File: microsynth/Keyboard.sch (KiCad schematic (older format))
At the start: 54 parts, among them J5 Conn_01x02_Male, Q1 BC182, Q2 BC182L, SW1-DRIFT1 DRIFT, SW9 TRIGGER, U1 RC4136, U2 TL072, U3 4011, U4 4016, U5 LF347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

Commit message: Change switch footprints
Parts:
- SW9: footprint Buttons_Switches_ThroughHole:DP3T_Toggle -> Buttons_Switches_ThroughHole:L203011MS02Q
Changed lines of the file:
@@
 F 0 "SW9" H 2750 3850 50  0000 L CNN
 F 1 "TRIGGER" H 2750 3750 50  0000 L CNN
-F 2 "Buttons_Switches_ThroughHole:DP3T_Toggle" H 2550 3700 50  0001 C CNN
+F 2 "Buttons_Switches_ThroughHole:L203011MS02Q" H 2550 3700 50  0001 C CNN
 F 3 "" H 2550 3700 50  0001 C CNN
 	2    2550 3700

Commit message: Layout...-3
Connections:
- net +VSW: now also SW9.2; no longer SW9.6
- net TO_S9A_KEYBOARD_CONTROLLER: now also SW9.4; no longer SW9.8
- new net: SW9.1, SW9.3, U3.2
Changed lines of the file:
@@
 $EndComp
 $Comp
-L power:GND #PWR0200
+L power:GND #PWR?
 U 1 1 5E8D13DA
 P 5600 2850
-F 0 "#PWR0200" H 5600 2600 50  0001 C CNN
+F 0 "#PWR?" H 5600 2600 50  0001 C CNN
 F 1 "GND" H 5605 2677 50  0000 C CNN
 F 2 "" H 5600 2850 50  0001 C CNN
@@
 	1850 3350 1850 3200
 $Comp
-L power:+VSW #PWR0201
+L power:+VSW #PWR?
 U 1 1 5E8EF5B5
 P 1850 3200
-F 0 "#PWR0201" H 1850 3050 50  0001 C CNN
+F 0 "#PWR?" H 1850 3050 50  0001 C CNN
 F 1 "+VSW" H 1865 3373 50  0000 C CNN
 F 2 "" H 1850 3200 50  0001 C CNN
@@
 	1200 2250 1300 2250
 $Comp
-L power:GND #PWR0202
+L power:GND #PWR?
 U 1 1 5E8F614B
 P 850 2350
-F 0 "#PWR0202" H 850 2100 50  0001 C CNN
+F 0 "#PWR?" H 850 2100 50  0001 C CNN
 F 1 "GND" H 855 2177 50  0000 C CNN
 F 2 "" H 850 2350 50  0001 C CNN
@@
 Connection ~ 850  2250
 $Comp
-L power:+VSW #PWR0203
+L power:+VSW #PWR?
 U 1 1 5E8F7B80
 P 850 2750
-F 0 "#PWR0203" H 850 2600 50  0001 C CNN
+F 0 "#PWR?" H 850 2600 50  0001 C CNN
 F 1 "+VSW" H 865 2923 50  0000 C CNN
 F 2 "" H 850 2750 50  0001 C CNN
@@
 $EndComp
 $Comp
-L power:GND #PWR0204
+L power:GND #PWR?
 U 1 1 5E8F97A9
 P 850 3500
-F 0 "#PWR0204" H 850 3250 50  0001 C CNN
+F 0 "#PWR?" H 850 3250 50  0001 C CNN
 F 1 "GND" H 855 3327 50  0000 C CNN
 F 2 "" H 850 3500 50  0001 C CNN
@@
 Connection ~ 5600 2150
 $Comp
-L power:GND #PWR0205
+L power:GND #PWR?
 U 1 1 5E9133C8
 P 900 850
-F 0 "#PWR0205" H 900 600 50  0001 C CNN
+F 0 "#PWR?" H 900 600 50  0001 C CNN
 F 1 "GND" H 905 677 50  0000 C CNN
 F 2 "" H 900 850 50  0001 C CNN
@@
 	900  850  1300 850
 $Comp
-L power:-VSW #PWR0206
+L power:-VSW #PWR?
 U 1 1 5E914B3C
 P 800 1250
-F 0 "#PWR0206" H 800 1350 50  0001 C CNN
+F 0 "#PWR?" H 800 1350 50  0001 C CNN
 F 1 "-VSW" H 815 1423 50  0000 C CNN
 F 2 "" H 800 1250 50  0001 C CNN
@@
 $EndComp
 $Comp
-L power:+VSW #PWR0207
+L power:+VSW #PWR?
 U 1 1 5E91C344
 P 4850 850
-F 0 "#PWR0207" H 4850 700 50  0001 C CNN
+F 0 "#PWR?" H 4850 700 50  0001 C CNN
 F 1 "+VSW" H 4865 1023 50  0000 C CNN
 F 2 "" H 4850 850 50  0001 C CNN
@@
 	6000 1250 5800 1250
 $Comp
-L power:-VSW #PWR0208
+L power:-VSW #PWR?
 U 1 1 5E92F178
 P 6750 1000
-F 0 "#PWR0208" H 6750 1100 50  0001 C CNN
+F 0 "#PWR?" H 6750 1100 50  0001 C CNN
 F 1 "-VSW" H 6765 1173 50  0000 C CNN
 F 2 "" H 6750 1000 50  0001 C CNN
@@
 	7000 1300 7000 1350
 $Comp
-L power:+VSW #PWR0209
+L power:+VSW #PWR?
 U 1 1 5E93EA0A
 P 7450 1000
-F 0 "#PWR0209" H 7450 850 50  0001 C CNN
+F 0 "#PWR?" H 7450 850 50  0001 C CNN
 F 1 "+VSW" H 7465 1173 50  0000 C CNN
 F 2 "" H 7450 1000 50  0001 C CNN
@@
 	7000 2000 7000 1800
 $Comp
-L power:GND #PWR0210
+L power:GND #PWR?
 U 1 1 5E94D6E3
 P 9000 1950
-F 0 "#PWR0210" H 9000 1700 50  0001 C CNN
+F 0 "#PWR?" H 9000 1700 50  0001 C CNN
 F 1 "GND" H 9005 1777 50  0000 C CNN
 F 2 "" H 9000 1950 50  0001 C CNN
@@
 Connection ~ 9400 1900
 $Comp
-L power:-VSW #PWR0211
+L power:-VSW #PWR?
 U 1 1 5E956780
 P 9400 850
-F 0 "#PWR0211" H 9400 950 50  0001 C CNN
+F 0 "#PWR?" H 9400 950 50  0001 C CNN
 F 1 "-VSW" H 9415 1023 50  0000 C CNN
 F 2 "" H 9400 850 50  0001 C CNN
@@
 	10250 2500 10400 2500
 $Comp
-L power:GND #PWR0212
+L power:GND #PWR?
 U 1 1 5E9679B4
 P 9950 3350
-F 0 "#PWR0212" H 9950 3100 50  0001 C CNN
+F 0 "#PWR?" H 9950 3100 50  0001 C CNN
 F 1 "GND" H 9955 3177 50  0000 C CNN
 F 2 "" H 9950 3350 50  0001 C CNN
@@
 	6850 3550 6850 3650
 $Comp
-L power:GND #PWR0213
+L power:GND #PWR?
 U 1 1 5E9F4545
 P 7250 3700
-F 0 "#PWR0213" H 7250 3450 50  0001 C CNN
+F 0 "#PWR?" H 7250 3450 50  0001 C CNN
 F 1 "GND" H 7255 3527 50  0000 C CNN
 F 2 "" H 7250 3700 50  0001 C CNN
@@
 Connection ~ 6400 3550
 $Comp
-L power:-VSW #PWR0214
+L power:-VSW #PWR?
 U 1 1 5EA12F1F
 P 6850 4500
-F 0 "#PWR0214" H 6850 4600 50  0001 C CNN
+F 0 "#PWR?" H 6850 4600 50  0001 C CNN
 F 1 "-VSW" H 6865 4673 50  0000 C CNN
 F 2 "" H 6850 4500 50  0001 C CNN
@@
 	6850 4500 6850 4450
 $Comp
-L power:+VSW #PWR0215
+L power:+VSW #PWR?
 U 1 1 5EA199A7
 P 6850 2700
-F 0 "#PWR0215" H 6850 2550 50  0001 C CNN
+F 0 "#PWR?" H 6850 2550 50  0001 C CNN
 F 1 "+VSW" H 6865 2873 50  0000 C CNN
 F 2 "" H 6850 2700 50  0001 C CNN
@@
 	6850 2700 6850 2800
 $Comp
-L power:GND #PWR0216
+L power:GND #PWR?
 U 1 1 5EA216DE
 P 7400 2700
-F 0 "#PWR0216" H 7400 2450 50  0001 C CNN
+F 0 "#PWR?" H 7400 2450 50  0001 C CNN
 F 1 "GND" H 7405 2527 50  0000 C CNN
 F 2 "" H 7400 2700 50  0001 C CNN
@@
 Connection ~ 8150 2350
 $Comp
-L power:+VSW #PWR0217
+L power:+VSW #PWR?
 U 1 1 5EA466FB
 P 4750 2500
-F 0 "#PWR0217" H 4750 2350 50  0001 C CNN
+F 0 "#PWR?" H 4750 2350 50  0001 C CNN
 F 1 "+VSW" H 4765 2673 50  0000 C CNN
 F 2 "" H 4750 2500 50  0001 C CNN
@@
 $EndComp
 $Comp
-L power:-VSW #PWR0218
+L power:-VSW #PWR?
 U 1 1 5EA46F8D
 P 4750 2800
-F 0 "#PWR0218" H 4750 2900 50  0001 C CNN
+F 0 "#PWR?" H 4750 2900 50  0001 C CNN
 F 1 "-VSW" H 4765 2973 50  0000 C CNN
 F 2 "" H 4750 2800 50  0001 C CNN
@@
 NoConn ~ 8750 2800
 $Comp
-L power:-VSW #PWR0219
+L power:-VSW #PWR?
 U 1 1 5EA96E7C
 P 8550 2800
-F 0 "#PWR0219" H 8550 2900 50  0001 C CNN
+F 0 "#PWR?" H 8550 2900 50  0001 C CNN
 F 1 "-VSW" H 8565 2973 50  0000 C CNN
 F 2 "" H 8550 2800 50  0001 C CNN
@@
 $EndComp
 $Comp
-L power:+VSW #PWR0220
+L power:+VSW #PWR?
 U 1 1 5EA97787
 P 8550 2200
-F 0 "#PWR0220" H 8550 2050 50  0001 C CNN
+F 0 "#PWR?" H 8550 2050 50  0001 C CNN
 F 1 "+VSW" H 8565 2373 50  0000 C CNN
 F 2 "" H 8550 2200 50  0001 C CNN
@@
 $Comp
 L microsynth-rescue:SW_DPTT_SELECTOR-Switch SW9
-U 2 1 5E96003B
+U 1 1 5E96003B
 P 2550 3700
 F 0 "SW9" H 2750 3850 50  0000 L CNN
@@
 F 2 "Buttons_Switches_ThroughHole:L203011MS02Q" H 2550 3700 50  0001 C CNN
 F 3 "" H 2550 3700 50  0001 C CNN
-	2    2550 3700
-	1    0    0    -1
+	1    2550 3700
+	1    0    0    1
 $EndComp
 $Comp
@@
 $EndComp
 $Comp
-L power:+VSW #PWR0232
+L power:+VSW #PWR?
 U 1 1 5E896D52
 P 9200 4350
-F 0 "#PWR0232" H 9200 4200 50  0001 C CNN
+F 0 "#PWR?" H 9200 4200 50  0001 C CNN
 F 1 "+VSW" H 9200 4450 50  0000 C CNN
 F 2 "" H 9200 4350 50  0001 C CNN
@@
 $EndComp
 $Comp
-L power:-VSW #PWR0233
+L power:-VSW #PWR?
 U 1 1 5E8967F9
 P 9200 5050
-F 0 "#PWR0233" H 9200 5150 50  0001 C CNN
+F 0 "#PWR?" H 9200 5150 50  0001 C CNN
 F 1 "-VSW" H 9215 5223 50  0000 C CNN
 F 2 "" H 9200 5050 50  0001 C CNN
@@
 Connection ~ 6400 2250
 $Comp
-L power:+VSW #PWR0234
+L power:+VSW #PWR?
 U 1 1 5E8EBE3F
 P 9650 4400
-F 0 "#PWR0234" H 9650 4250 50  0001 C CNN
+F 0 "#PWR?" H 9650 4250 50  0001 C CNN
 F 1 "+VSW" H 9650 4500 50  0000 C CNN
 F 2 "" H 9650 4400 50  0001 C CNN
@@
 $EndComp
 $Comp
-L power:-VSW #PWR0235
+L power:-VSW #PWR?
 U 1 1 5E8EC49A
 P 9650 5000
-F 0 "#PWR0235" H 9650 5100 50  0001 C CNN
+F 0 "#PWR?" H 9650 5100 50  0001 C CNN
 F 1 "-VSW" H 9665 5173 50  0000 C CNN
 F 2 "" H 9650 5000 50  0001 C CNN
@@
 $EndComp
 $Comp
-L power:+VSW #PWR0236
+L power:+VSW #PWR?
 U 1 1 5EC4CC4F
 P 10050 4400
-F 0 "#PWR0236" H 10050 4250 50  0001 C CNN
+F 0 "#PWR?" H 10050 4250 50  0001 C CNN
 F 1 "+VSW" H 10050 4500 50  0000 C CNN
 F 2 "" H 10050 4400 50  0001 C CNN
@@
 $EndComp
 $Comp
-L power:-VSW #PWR0237
+L power:-VSW #PWR?
 U 1 1 5EC4D1BE
 P 10050 5000
-F 0 "#PWR0237" H 10050 5100 50  0001 C CNN
+F 0 "#PWR?" H 10050 5100 50  0001 C CNN
 F 1 "-VSW" H 10065 5173 50  0000 C CNN
 F 2 "" H 10050 5000 50  0001 C CNN
@@
 	8150 2150 8150 2350
 $Comp
-L power:-VSW #PWR0228
+L power:-VSW #PWR?
 U 1 1 5E98AA20
 P 6350 1000
-F 0 "#PWR0228" H 6350 1100 50  0001 C CNN
+F 0 "#PWR?" H 6350 1100 50  0001 C CNN
 F 1 "-VSW" H 6365 1173 50  0000 C CNN
 F 2 "" H 6350 1000 50  0001 C CNN
@@
 $EndComp
 $Comp
-L power:-VSW #PWR0229
+L power:-VSW #PWR?
 U 1 1 5E98AE00
 P 6550 1000
-F 0 "#PWR0229" H 6550 1100 50  0001 C CNN
+F 0 "#PWR?" H 6550 1100 50  0001 C CNN
 F 1 "-VSW" H 6565 1173 50  0000 C CNN
 F 2 "" H 6550 1000 50  0001 C CNN

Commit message: Tidy up, name switches, proper footprints for all trimmers
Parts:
- SW1-DRIFT1, SW9: footprint Buttons_Switches_ThroughHole:L203011MS02Q -> Buttons_Switches_ThroughHole:G-1128S-1110
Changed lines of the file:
@@
 F 0 "SW1" H 5844 1083 50  0000 L CNN
 F 1 "DRIFT" H 5844 992 50  0000 L CNN
-F 2 "Buttons_Switches_ThroughHole:L203011MS02Q" H 5650 1050 50  0001 C CNN
+F 2 "Buttons_Switches_ThroughHole:G-1128S-1110" H 5650 1050 50  0001 C CNN
 F 3 "https://www.tme.eu/Document/aa2d40399ed88e2cc02320a01dfb97ce/OSseries.pdf" H 5650 1050 50  0001 C CNN
 F 4 "DRIFT" H 5844 901 50  0000 L CNN "Label"
@@
 F 0 "SW9" H 2750 3850 50  0000 L CNN
 F 1 "TRIGGER" H 2750 3750 50  0000 L CNN
-F 2 "Buttons_Switches_ThroughHole:L203011MS02Q" H 2550 3700 50  0001 C CNN
+F 2 "Buttons_Switches_ThroughHole:G-1128S-1110" H 2550 3700 50  0001 C CNN
 F 3 "" H 2550 3700 50  0001 C CNN
 	1    2550 3700

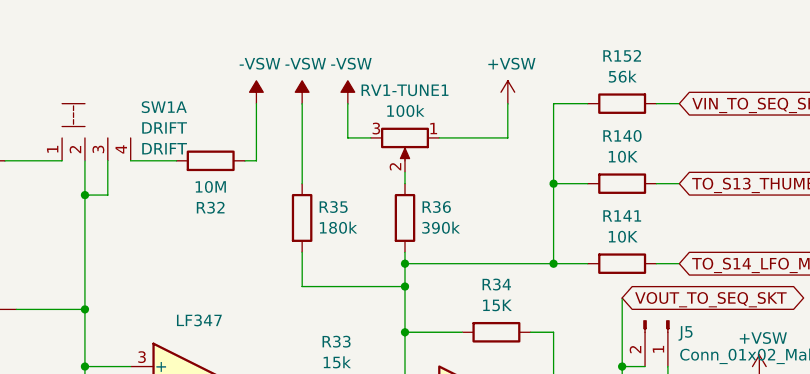
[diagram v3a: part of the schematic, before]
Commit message: Replace switches in schematic, add extra octave to VCO
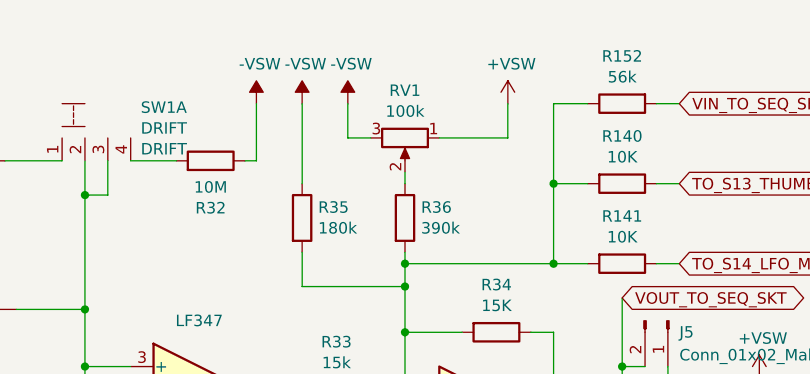
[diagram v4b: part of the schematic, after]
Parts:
- renumbered RV1-TUNE1 to RV1
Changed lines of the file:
@@
 	7000 1800 7000 1700
 $Comp
-L Device:R_POT RV1-TUNE1
+L Device:R_POT RV1
 U 1 1 5E936F79
 P 7000 1150
-F 0 "RV1-TUNE1" V 6793 1150 50  0000 C CNN
+F 0 "RV1" V 6793 1150 50  0000 C CNN
 F 1 "100k" V 6884 1150 50  0000 C CNN
 F 2 "Potentiometers:Potentiometer_Trimmer_Bourns_PV36W" H 7000 1150 50  0001 C CNN

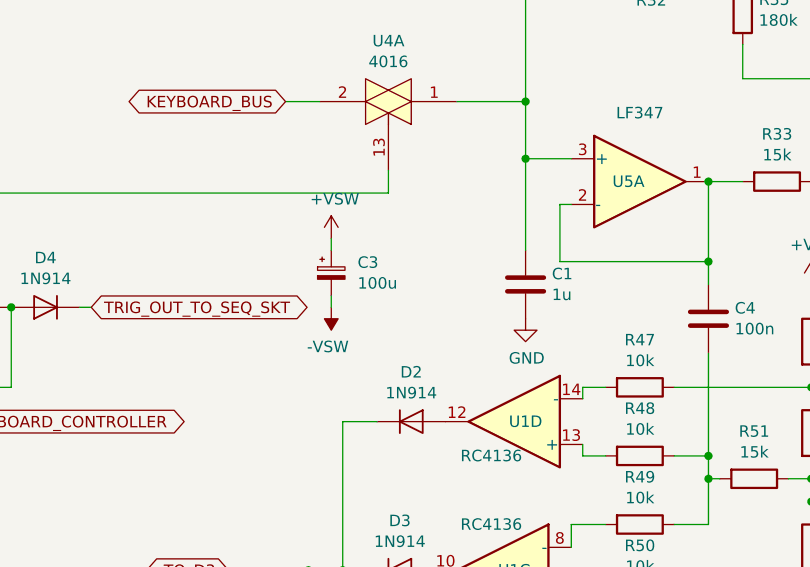
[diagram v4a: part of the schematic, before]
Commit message: Proper capacitor footprints
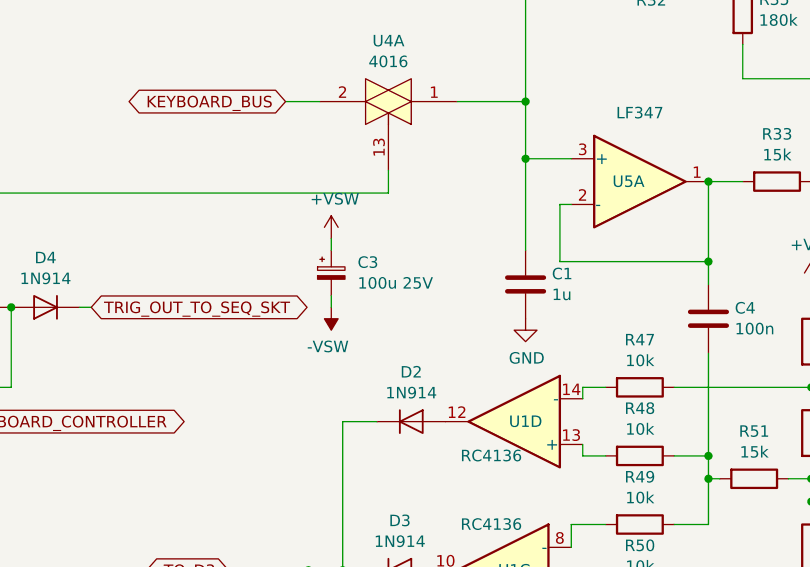
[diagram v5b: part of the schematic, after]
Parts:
- C1: footprint Capacitor_THT:C_Disc_D5.0mm_W2.5mm_P5.00mm -> Capacitor_THT:C_Rect_L7.2mm_W7.2mm_P5.00mm_FKS2_FKP2_MKS2_MKP2
- C2, C4, C6, C7: footprint Capacitor_THT:C_Disc_D5.0mm_W2.5mm_P5.00mm -> Capacitor_THT:C_Rect_L7.2mm_W2.5mm_P5.00mm_FKS2_FKP2_MKS2_MKP2
- C3: value 100u -> 100u 25V
- C5: footprint Capacitor_THT:C_Disc_D5.0mm_W2.5mm_P5.00mm -> Capacitor_THT:C_Rect_L7.2mm_W4.5mm_P5.00mm_FKS2_FKP2_MKS2_MKP2
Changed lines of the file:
@@
 F 0 "C6" H 9815 1696 50  0000 L CNN
 F 1 "10n" H 9815 1605 50  0000 L CNN
-F 2 "Capacitor_THT:C_Disc_D5.0mm_W2.5mm_P5.00mm" H 9738 1500 50  0001 C CNN
+F 2 "Capacitor_THT:C_Rect_L7.2mm_W2.5mm_P5.00mm_FKS2_FKP2_MKS2_MKP2" H 9738 1500 50  0001 C CNN
 F 3 "~" H 9700 1650 50  0001 C CNN
 	1    9700 1650
@@
 F 0 "C7" H 10365 2946 50  0000 L CNN
 F 1 "100n" H 10365 2855 50  0000 L CNN
-F 2 "Capacitor_THT:C_Disc_D5.0mm_W2.5mm_P5.00mm" H 10288 2750 50  0001 C CNN
+F 2 "Capacitor_THT:C_Rect_L7.2mm_W2.5mm_P5.00mm_FKS2_FKP2_MKS2_MKP2" H 10288 2750 50  0001 C CNN
 F 3 "~" H 10250 2900 50  0001 C CNN
 	1    10250 2900
@@
 F 0 "C5" V 7548 2700 50  0000 C CNN
 F 1 "470n" V 7639 2700 50  0000 C CNN
-F 2 "Capacitor_THT:C_Disc_D5.0mm_W2.5mm_P5.00mm" H 7838 2550 50  0001 C CNN
+F 2 "Capacitor_THT:C_Rect_L7.2mm_W4.5mm_P5.00mm_FKS2_FKP2_MKS2_MKP2" H 7838 2550 50  0001 C CNN
 F 3 "~" H 7800 2700 50  0001 C CNN
 	1    7800 2700
@@
 F 0 "C4" H 6515 2896 50  0000 L CNN
 F 1 "100n" H 6515 2805 50  0000 L CNN
-F 2 "Capacitor_THT:C_Disc_D5.0mm_W2.5mm_P5.00mm" H 6438 2700 50  0001 C CNN
+F 2 "Capacitor_THT:C_Rect_L7.2mm_W2.5mm_P5.00mm_FKS2_FKP2_MKS2_MKP2" H 6438 2700 50  0001 C CNN
 F 3 "~" H 6400 2850 50  0001 C CNN
 	1    6400 2850
@@
 F 0 "C1" H 5715 2746 50  0000 L CNN
 F 1 "1u" H 5715 2655 50  0000 L CNN
-F 2 "Capacitor_THT:C_Disc_D5.0mm_W2.5mm_P5.00mm" H 5638 2550 50  0001 C CNN
+F 2 "Capacitor_THT:C_Rect_L7.2mm_W7.2mm_P5.00mm_FKS2_FKP2_MKS2_MKP2" H 5638 2550 50  0001 C CNN
 F 3 "~" H 5600 2700 50  0001 C CNN
 	1    5600 2700
@@
 F 0 "C2" V 798 1900 50  0000 C CNN
 F 1 "22n" V 889 1900 50  0000 C CNN
-F 2 "Capacitor_THT:C_Disc_D5.0mm_W2.5mm_P5.00mm" H 1088 1750 50  0001 C CNN
+F 2 "Capacitor_THT:C_Rect_L7.2mm_W2.5mm_P5.00mm_FKS2_FKP2_MKS2_MKP2" H 1088 1750 50  0001 C CNN
 F 3 "~" H 1050 1900 50  0001 C CNN
 	1    1050 1900
@@
 	1    4750 2800
 	-1   0    0    1
-$EndComp
-$Comp
-L Device:CP_Small C3
-U 1 1 5EA4781A
-P 4750 2650
-F 0 "C3" H 4865 2696 50  0000 L CNN
-F 1 "100u" H 4865 2605 50  0000 L CNN
-F 2 "Capacitor_THT:CP_Radial_D5.0mm_P2.50mm" H 4788 2500 50  0001 C CNN
-F 3 "~" H 4750 2650 50  0001 C CNN
-	1    4750 2650
-	1    0    0    -1
 $EndComp
 Wire Wire Line
@@
 Wire Wire Line
 	9700 3600 10400 3600
+$Comp
+L Device:CP_Small C3
+U 1 1 5EA4781A
+P 4750 2650
+F 0 "C3" H 4865 2696 50  0000 L CNN
+F 1 "100u 25V" H 4865 2605 50  0000 L CNN
+F 2 "Capacitor_THT:CP_Radial_D5.0mm_P2.50mm" H 4788 2500 50  0001 C CNN
+F 3 "~" H 4750 2650 50  0001 C CNN
+	1    4750 2650
+	1    0    0    -1
+$EndComp
 $EndSCHEMATC

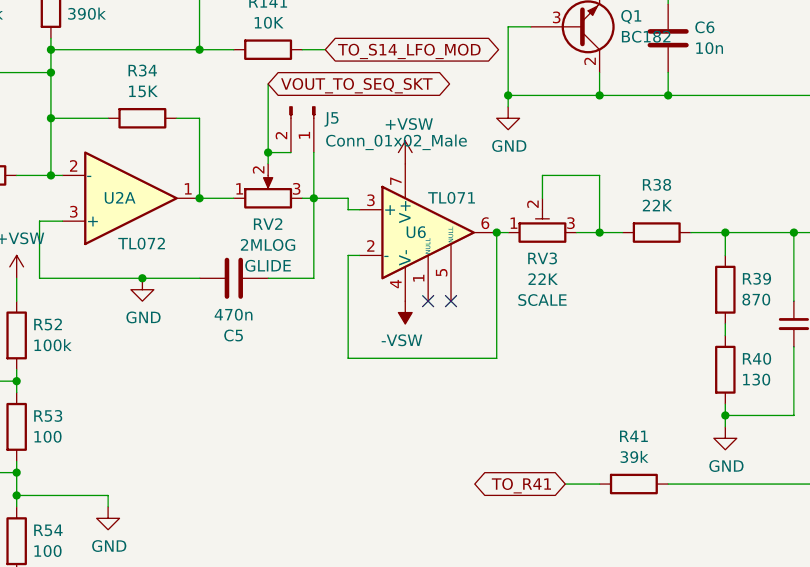
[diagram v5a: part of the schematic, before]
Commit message: Label pots
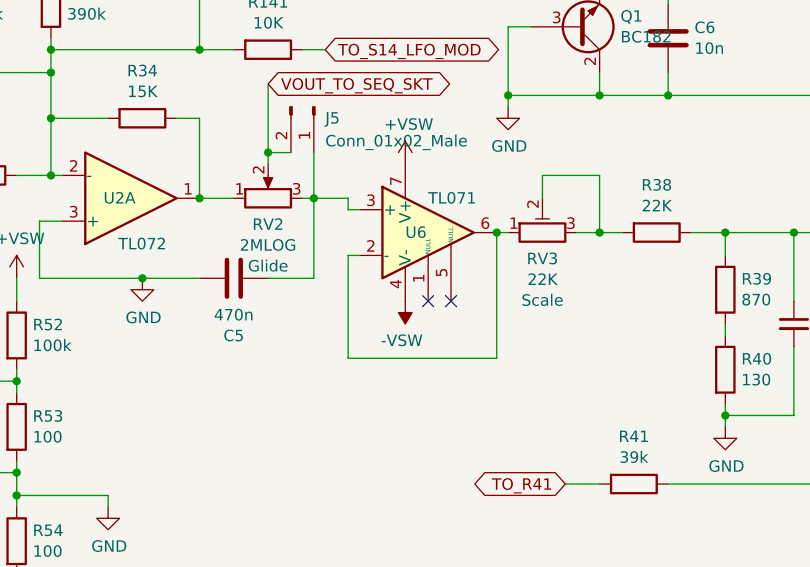
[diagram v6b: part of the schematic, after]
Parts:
- RV2: Label GLIDE -> Glide
- RV3: Label SCALE -> Scale
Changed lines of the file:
@@
 F 2 "Potentiometers:Potentiometer_Trimmer_Bourns_PV36W" H 9150 2500 50  0001 C CNN
 F 3 "~" H 9150 2500 50  0001 C CNN
-F 4 "SCALE" V 8853 2500 50  0000 C CNN "Label"
+F 4 "Scale" V 8853 2500 50  0000 C CNN "Label"
 	1    9150 2500
 	0    -1   -1   0
@@
 F 2 "4ms_Potentiometer:Pot_16mm_NoDet_RV16AF-4A" H 7950 2350 50  0001 C CNN
 F 3 "~" H 7950 2350 50  0001 C CNN
-F 4 "GLIDE" V 7653 2350 50  0000 C CNN "Label"
+F 4 "Glide" V 7653 2350 50  0000 C CNN "Label"
 	1    7950 2350
 	0    -1   -1   0

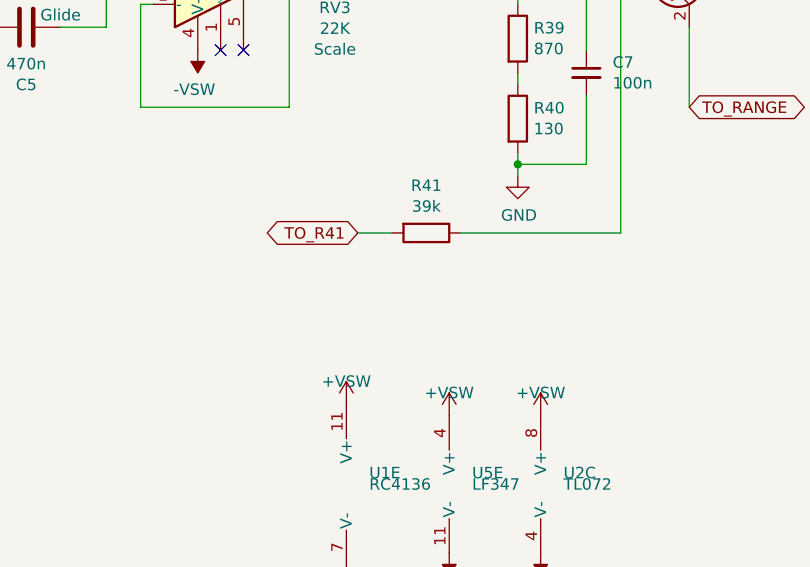
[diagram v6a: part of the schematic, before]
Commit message: Add new V input
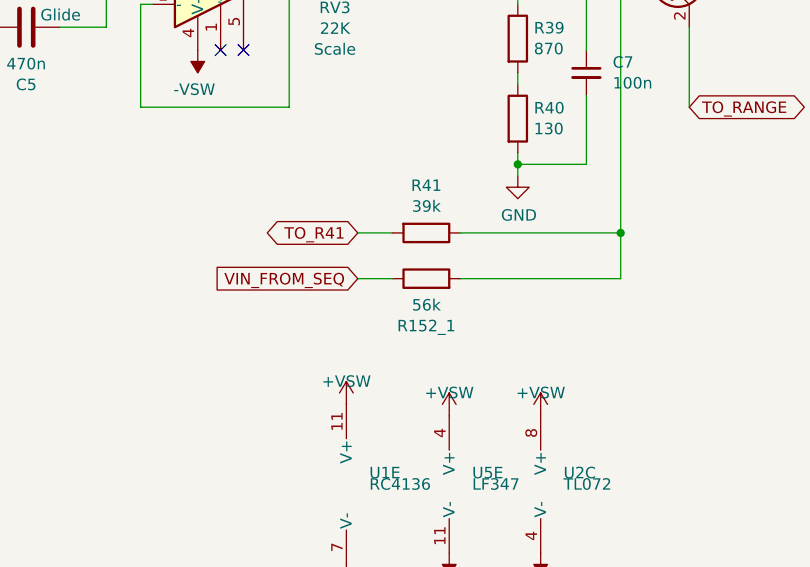
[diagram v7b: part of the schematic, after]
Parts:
- added R152_1: 56k, Resistor_THT:R_Axial_DIN0207_L6.3mm_D2.5mm_P10.16mm_Horizontal, symbol Device:R
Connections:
- net at C7.1, Q2.3 (B), R38.1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: now also R152_1.2
- new net VIN_FROM_SEQ: R152_1.1
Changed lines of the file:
@@
 	1    0    0    -1
 $EndComp
+Text GLabel 9250 3800 0    50   Input ~ 0
+VIN_FROM_SEQ
+$Comp
+L Device:R R152_1
+U 1 1 5EB8A8FE
+P 9550 3800
+F 0 "R152_1" V 9343 3800 50  0000 C CNN
+F 1 "56k" V 9434 3800 50  0000 C CNN
+F 2 "Resistor_THT:R_Axial_DIN0207_L6.3mm_D2.5mm_P10.16mm_Horizontal" V 9480 3800 50  0001 C CNN
+F 3 "~" H 9550 3800 50  0001 C CNN
+	1    9550 3800
+	0    -1   -1   0
+$EndComp
+Wire Wire Line
+	9700 3800 10400 3800
+Wire Wire Line
+	10400 3800 10400 3600
+Connection ~ 10400 3600
+Wire Wire Line
+	9400 3800 9250 3800
 $EndSCHEMATC
